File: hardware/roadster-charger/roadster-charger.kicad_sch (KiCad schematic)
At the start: 63 parts, among them J1 USB4505-03-0-A, J2 USB4505-03-0-A, J3 54-00166, Q1 CSD19532Q5B, U1 MPM3606AGQV-P, U2 ESP32-C3-MINI-1, U3 INA168, U4 OPA340NA, U5 FUSB307BMPX, U6 LM75B, U7 LM5050-1, U8 INA168, U9 OPA340NA

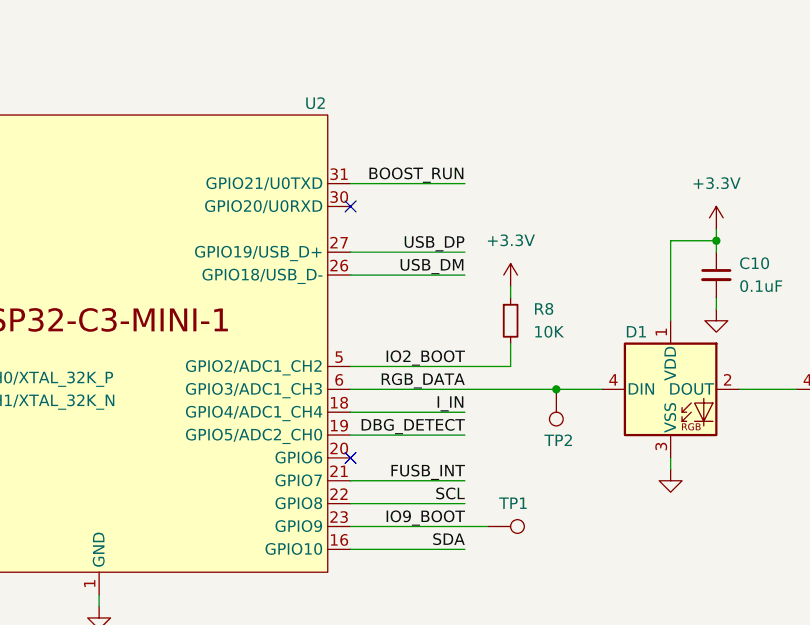
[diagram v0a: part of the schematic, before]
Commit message: Rough rev 2 layout
Move boost run pin to GPIO6 to avoid hard coded UART output
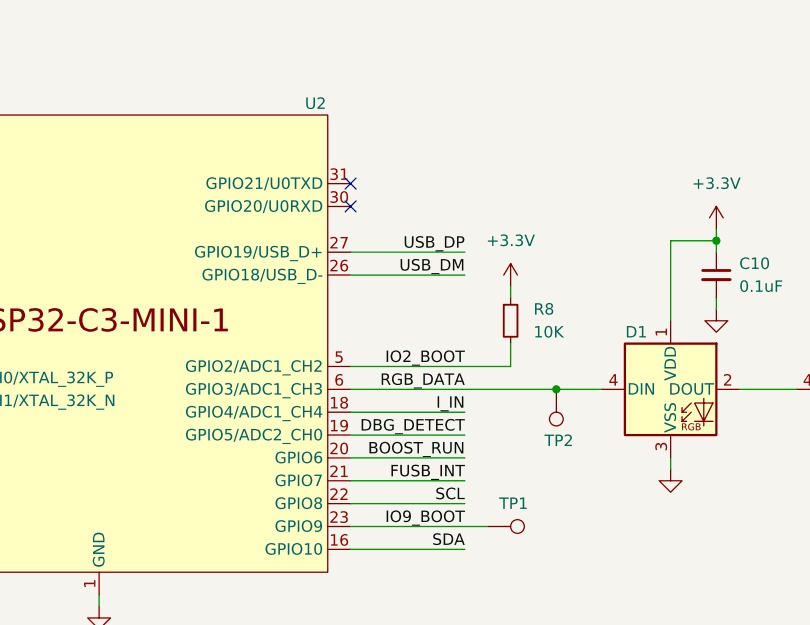
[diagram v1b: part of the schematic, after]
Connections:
- net BOOST_RUN: now also U2.20 (GPIO6); no longer U2.31 (GPIO21/U0TXD)
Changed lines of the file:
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@@
 	)
 	(no_connect
-		(at 96.52 227.33)
+		(at 96.52 196.85)
 	)
 	(no_connect
@@
 	(wire
 		(pts
-			(xy 96.52 196.85) (xy 109.22 196.85)
-		)
-		(stroke
-			(width 0)
-			(type default)
-		)
-	)
-	(wire
-		(pts
 			(xy 387.35 140.97) (xy 387.35 143.51)
 		)
@@
 	(wire
 		(pts
+			(xy 96.52 227.33) (xy 109.22 227.33)
+		)
+		(stroke
+			(width 0)
+			(type default)
+		)
+	)
+	(wire
+		(pts
 			(xy 36.83 241.3) (xy 36.83 238.76)
 		)
@@
 	)
 	(label "BOOST_RUN"
-		(at 109.22 196.85 180)
+		(at 109.22 227.33 180)
 		(fields_autoplaced yes)
 		(effects
@@
 			)
 		)
-		(property "Description" "\nConnector, dc jack 5.5x2.1 mm, PCB mount, 90 degrees, nickel plated, PBT, thru hole\n"
+		(property "Description" "Connector, dc jack 5.5x2.1 mm, PCB mount, 90 degrees, nickel plated, PBT, thru hole"
 			(at 393.7 140.97 0)
 			(effects

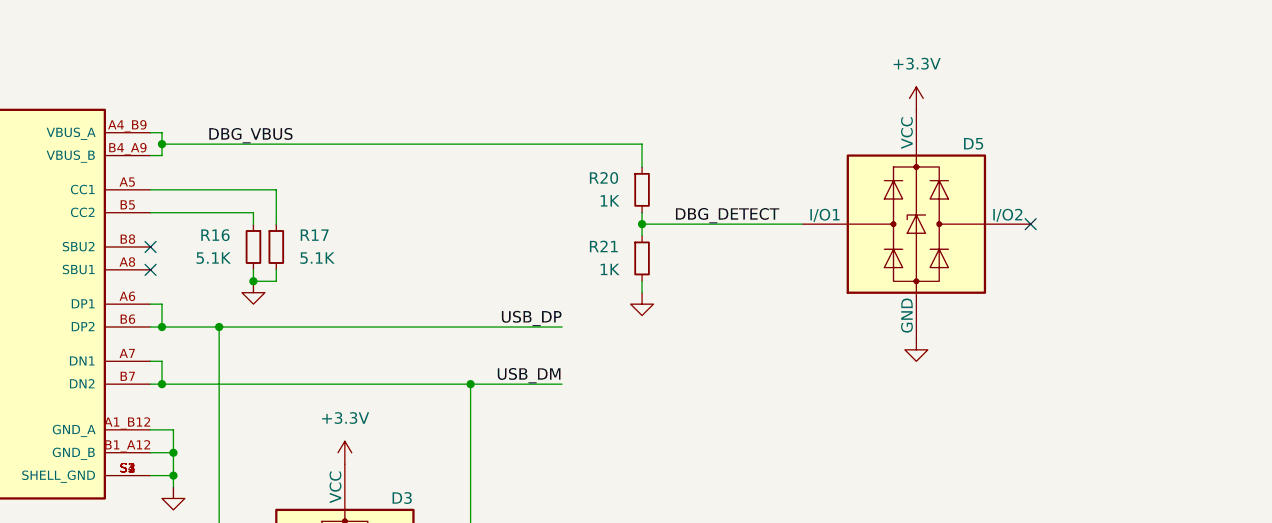
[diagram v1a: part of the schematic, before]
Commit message: add debug connected LED
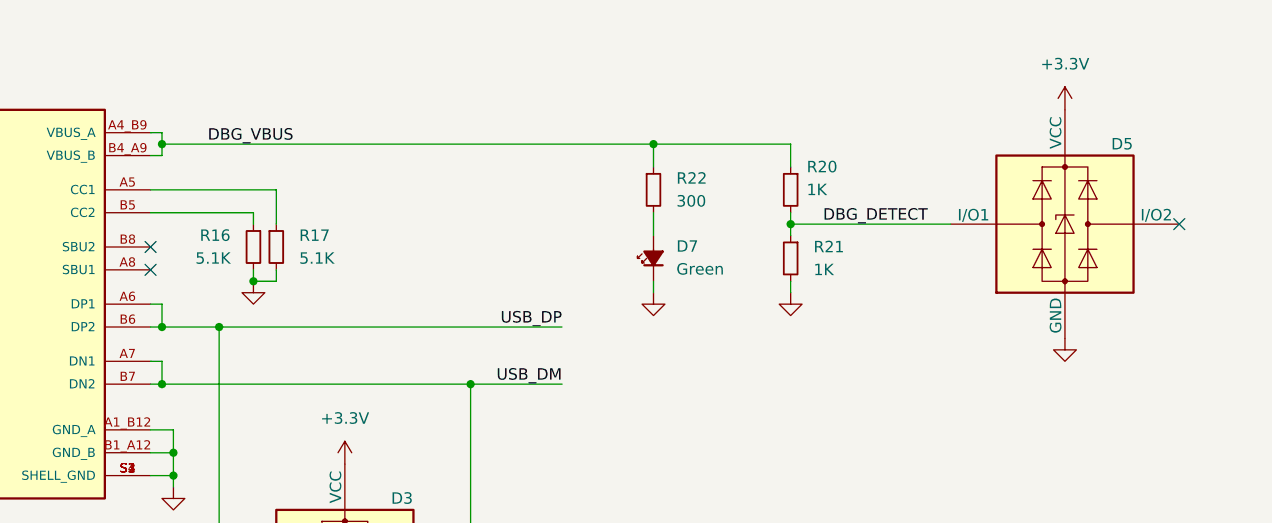
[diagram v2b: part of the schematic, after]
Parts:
- added D7: Green, LED_SMD:LED_0805_2012Metric, symbol Device:LED_Small_Filled
- added R22: 300, Resistor_SMD:R_0603_1608Metric, symbol Device:R_Small
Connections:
- net DBG_VBUS: now also R22.1
- net GND: now also D7.1 (K)
- new net: D7.2 (A), R22.2
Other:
- moved on the sheet: D5, R20, R21

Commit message: change all 1K Rs to 0.1%, invert DAC jumpers
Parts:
- R19, R20, R21: MPN RC0603FR-071KL -> RT0603BRD071KL
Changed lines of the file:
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@@
 			)
 		)
-		(property "MPN" "RC0603FR-071KL"
+		(property "MPN" "RT0603BRD071KL"
 			(at 360.68 36.83 0)
 			(effects
@@
 			)
 		)
-		(property "MPN" "RC0603FR-071KL"
+		(property "MPN" "RT0603BRD071KL"
 			(at 340.36 168.91 0)
 			(effects
@@
 			)
 		)
-		(property "MPN" "RC0603FR-071KL"
+		(property "MPN" "RT0603BRD071KL"
 			(at 360.68 44.45 0)
 			(effects

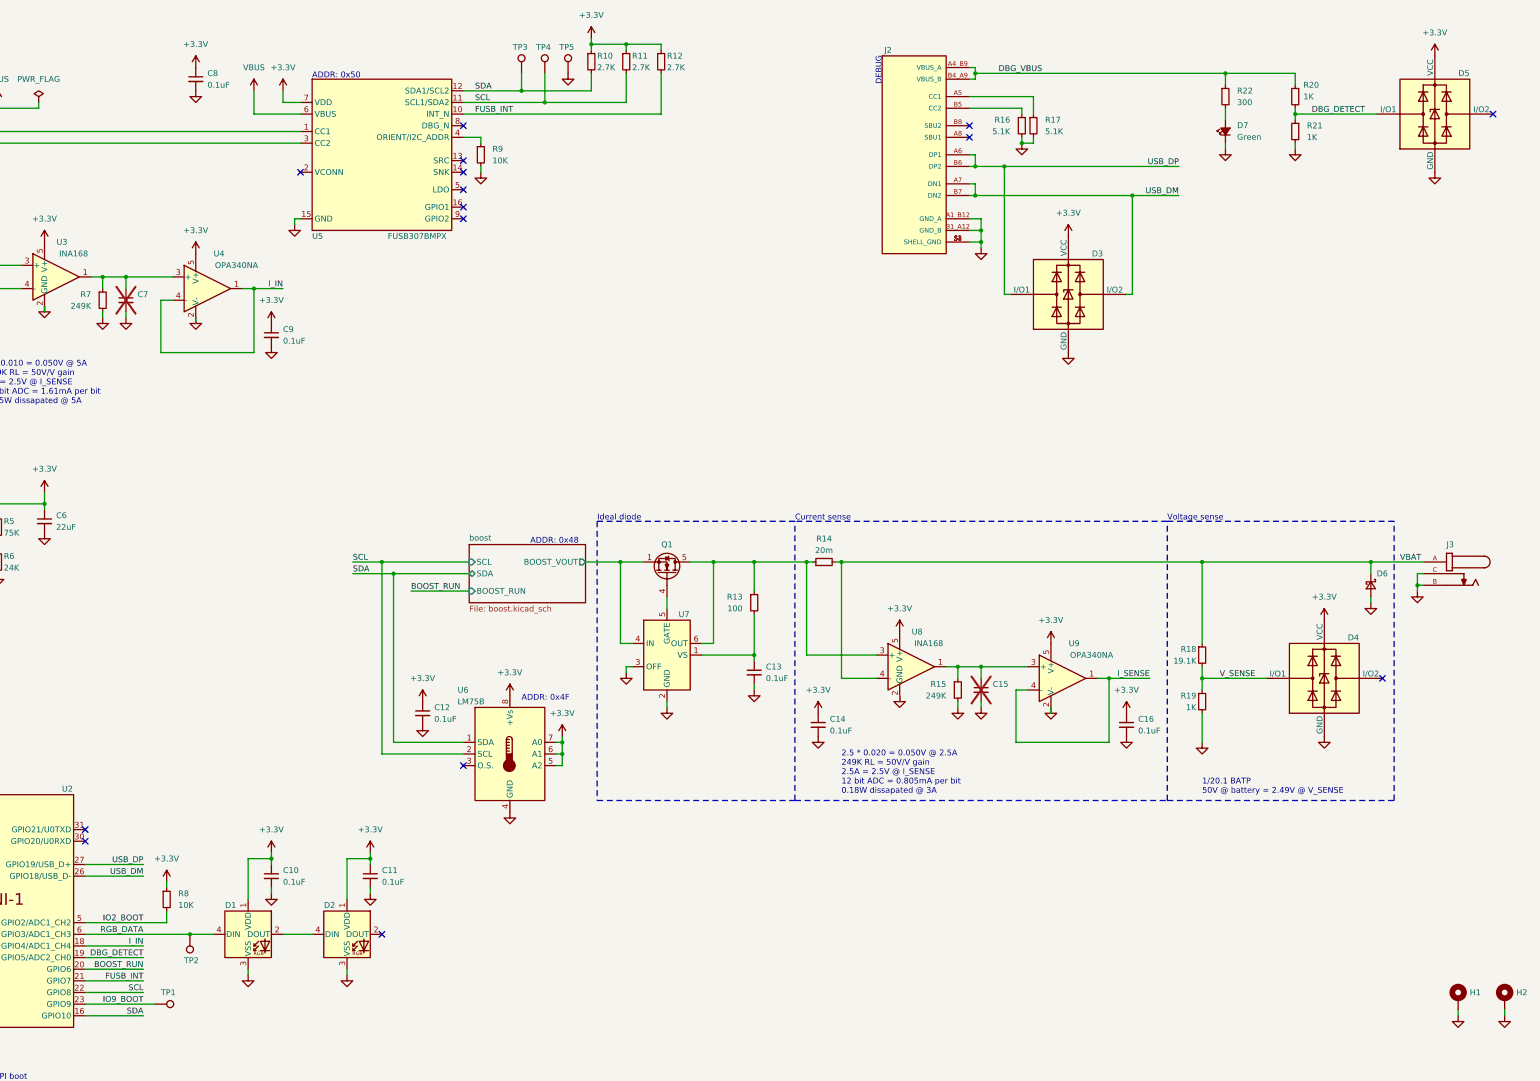
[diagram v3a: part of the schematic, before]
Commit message: reannotate, add uart test points
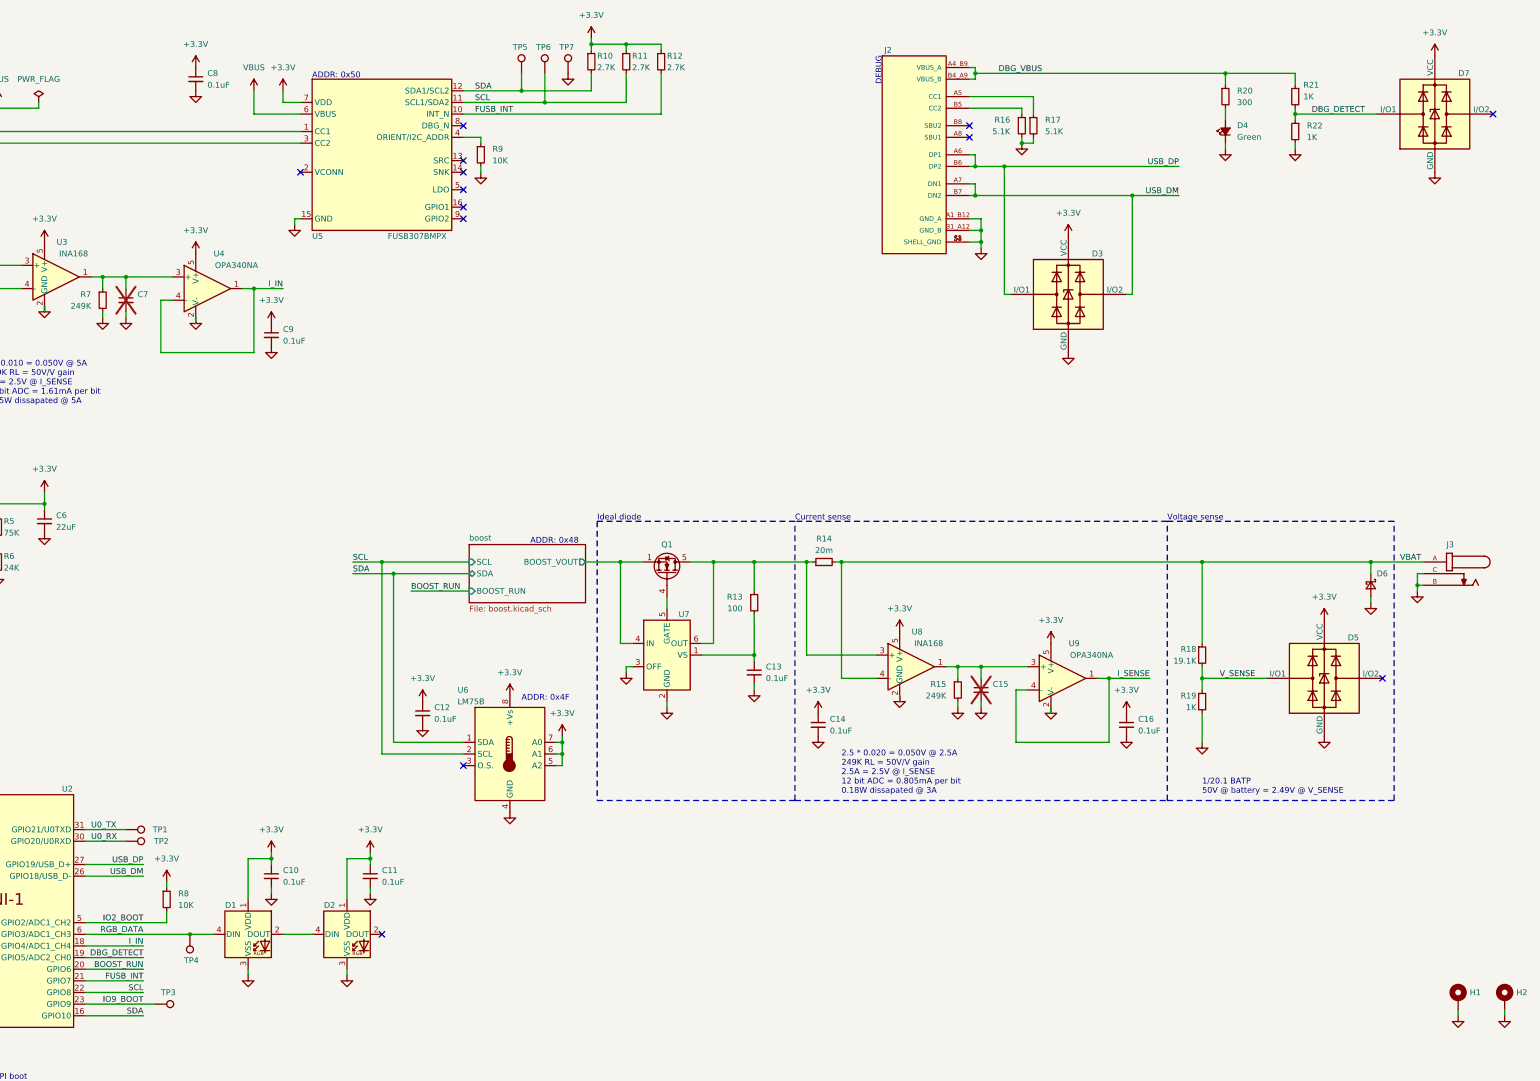
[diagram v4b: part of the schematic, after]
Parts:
- added TP1, TP2: RCU-0C, RCU-0C:TP+195X110, symbol Connector:TestPoint
- renumbered D7 to D4, D4 to D5, D5 to D7, R22 to R20, R20 to R21, R21 to R22, TP1 to TP3, TP2 to TP4, TP3 to TP5, TP4 to TP6, TP5 to TP7
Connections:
- net U0_RX: now reaches U2.30 (GPIO20/U0RXD)
- net U0_RX: now also TP2.1
- net U0_TX: now reaches U2.31 (GPIO21/U0TXD)
- net U0_TX: now also TP1.1
- no-connect marks 23 -> 21

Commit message: use track cleanup tool
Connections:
- net GND: no longer J1.S1 (SHELL_GND), J1.S2 (SHELL_GND), J1.S3 (SHELL_GND), J1.S4 (SHELL_GND), J2.S1 (SHELL_GND), J2.S2 (SHELL_GND), J2.S3 (SHELL_GND), J2.S4 (SHELL_GND)
- new net: J2.S1 (SHELL_GND), J2.S2 (SHELL_GND), J2.S3 (SHELL_GND), J2.S4 (SHELL_GND)
- new net: J1.S1 (SHELL_GND), J1.S2 (SHELL_GND), J1.S3 (SHELL_GND), J1.S4 (SHELL_GND)
- no-connect marks 21 -> 23
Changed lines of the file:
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@@
-	)
-	(junction
-		(at 292.1 68.58)
-		(diameter 0)
-		(color 0 0 0 0)
 	)
 	(junction
@@
 	(junction
 		(at 345.44 31.75)
-		(diameter 0)
-		(color 0 0 0 0)
-	)
-	(junction
-		(at 60.96 76.2)
 		(diameter 0)
 		(color 0 0 0 0)
@@
 	)
 	(no_connect
+		(at 58.42 76.2)
+	)
+	(no_connect
 		(at 179.07 60.96)
+	)
+	(no_connect
+		(at 289.56 68.58)
 	)
 	(no_connect
@@
 	(wire
 		(pts
-			(xy 60.96 76.2) (xy 60.96 77.47)
+			(xy 60.96 73.66) (xy 60.96 77.47)
 		)
 		(stroke
@@
 	(wire
 		(pts
-			(xy 292.1 66.04) (xy 292.1 68.58)
+			(xy 292.1 66.04) (xy 292.1 69.85)
 		)
 		(stroke
@@
 	(wire
 		(pts
-			(xy 289.56 68.58) (xy 292.1 68.58)
-		)
-		(stroke
-			(width 0)
-			(type default)
-		)
-	)
-	(wire
-		(pts
 			(xy 137.16 203.2) (xy 137.16 204.47)
 		)
@@
 		)
 		(stroke
-			(width 0)
-			(type default)
-		)
-	)
-	(wire
-		(pts
-			(xy 58.42 76.2) (xy 60.96 76.2)
-		)
-		(stroke
-			(width 0)
-			(type default)
-		)
-	)
-	(wire
-		(pts
-			(xy 292.1 68.58) (xy 292.1 69.85)
-		)
-		(stroke
-			(width 0)
-			(type default)
-		)
-	)
-	(wire
-		(pts
-			(xy 60.96 73.66) (xy 60.96 76.2)
-		)
-		(stroke

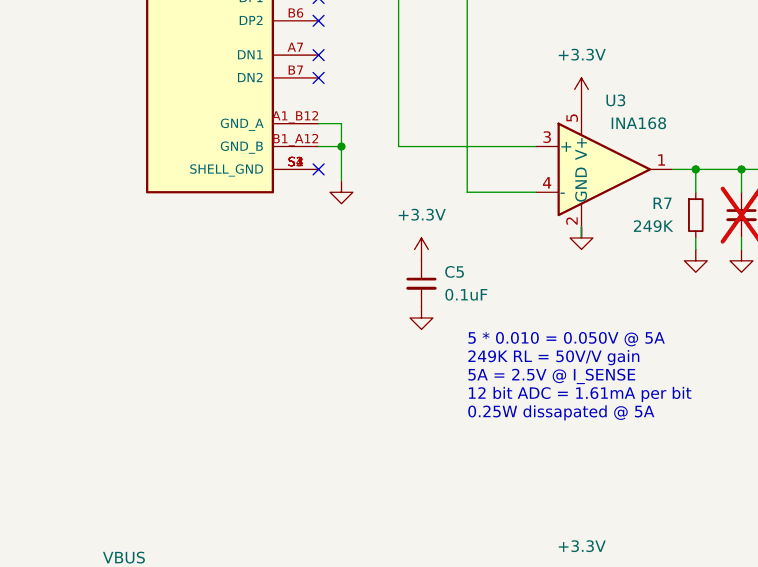
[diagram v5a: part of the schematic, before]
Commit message: ERC / DRC cleanup
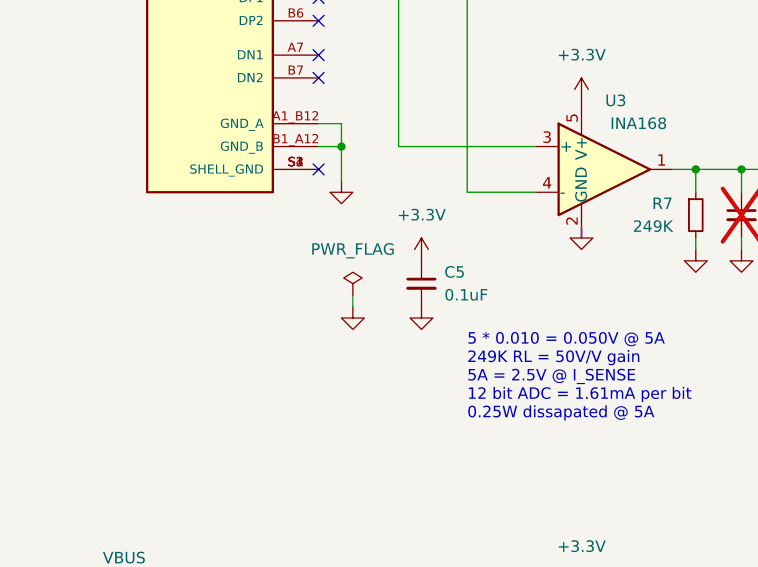
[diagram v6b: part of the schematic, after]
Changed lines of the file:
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@@
 		)
 	)
+	(wire
+		(pts
+			(xy 62.23 90.17) (xy 62.23 91.44)
+		)
+		(stroke
+			(width 0)
+			(type default)
+		)
+	)
 	(polyline
 		(pts
@@
 	)
 	(symbol
+		(lib_id "power:GND")
+		(at 62.23 91.44 0)
+		(unit 1)
+		(exclude_from_sim no)
+		(in_bom yes)
+		(on_board yes)
+		(dnp no)
+		(property "Reference" "#PWR089"
+			(at 62.23 97.79 0)
+			(effects
+				(font
+					(size 1.27 1.27)
+				)
+				(hide yes)
+			)
+		)
+		(property "Value" "GND"
+			(at 62.23 96.52 0)
+			(effects
+				(font
+					(size 1.27 1.27)
+				)
+				(hide yes)
+			)
+		)
+		(property "Footprint" ""
+			(at 62.23 91.44 0)
+			(effects
+				(font
+					(size 1.27 1.27)
+				)
+				(hide yes)
+			)
+		)
+		(property "Datasheet" ""
+			(at 62.23 91.44 0)
+			(effects
+				(font
+					(size 1.27 1.27)
+				)
+				(hide yes)
+			)
+		)
+		(property "Description" ""
+			(at 62.23 91.44 0)
+			(effects
+				(font
+					(size 1.27 1.27)
+				)
+				(hide yes)
+			)
+		)
+		(pin "1"
+		)
+		(instances
+			(project "roadster-charger"
+				(path "/57ecac41-cd8a-4182-a81e-fed3e381aedd"
+					(reference "#PWR089")
+					(unit 1)
+				)
+			)
+		)
+	)
+	(symbol
 		(lib_id "power:+3.3V")
 		(at 114.3 208.28 0)
@@
 	(symbol
 		(lib_id "power:PWR_FLAG")
+		(at 62.23 90.17 0)
+		(unit 1)
+		(exclude_from_sim no)
+		(in_bom yes)
+		(on_board yes)
+		(dnp no)
+		(fields_autoplaced yes)
+		(property "Reference" "#FLG02"
+			(at 62.23 88.265 0)
+			(effects
+				(font
+					(size 1.27 1.27)
+				)
+				(hide yes)
+			)
+		)
+		(property "Value" "PWR_FLAG"
+			(at 62.23 85.09 0)
+			(effects
+				(font
+					(size 1.27 1.27)
+				)
+			)
+		)
+		(property "Footprint" ""
+			(at 62.23 90.17 0)
+			(effects
+				(font
+					(size 1.27 1.27)
+				)
+				(hide yes)
+			)
+		)
+		(property "Datasheet" "~"
+			(at 62.23 90.17 0)
+			(effects
+				(font
+					(size 1.27 1.27)
+				)
+				(hide yes)
+			)
+		)
+		(property "Description" ""
+			(at 62.23 90.17 0)
+			(effects
+				(font
+					(size 1.27 1.27)
+				)
+				(hide yes)
+			)
+		)
+		(pin "1"
+		)
+		(instances
+			(project "roadster-charger"
+				(path "/57ecac41-cd8a-4182-a81e-fed3e381aedd"
+					(reference "#FLG02")
+					(unit 1)
+				)
+			)
+		)
+	)
+	(symbol
+		(lib_id "power:PWR_FLAG")
 		(at 86.36 38.1 0)
 		(unit 1)
@@
 	)
 	(symbol
+		(lib_name "WS2812B_1")
 		(lib_id "LED:WS2812B")
 		(at 132.08 219.71 0)

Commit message: Fix res PN, remove TPs from BOM, add DNPs to BOM
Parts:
- C15, C7: now in the parts list
- H1, H2: MPN (none) -> DNP
- R20: MPN (none) -> RC0603JR-07330RL; MPN  RC0603JR-07330RL -> (none)
- TP1, TP2, TP3, TP4, TP5, TP6, TP7: now left out of the parts list
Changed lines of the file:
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@@
 		(unit 1)
 		(exclude_from_sim no)
-		(in_bom yes)
+		(in_bom no)
 		(on_board yes)
 		(dnp no)
@@
 		(unit 1)
 		(exclude_from_sim no)
-		(in_bom yes)
+		(in_bom no)
 		(on_board yes)
 		(dnp no)
@@
 			)
 		)
-		(property "MPN " "RC0603JR-07330RL"
+		(property "MPN" "RC0603JR-07330RL"
 			(at 345.44 36.83 0)
 			(effects
@@
 			)
 		)
+		(property "MPN" "DNP"
+			(at 406.4 233.68 0)
+			(effects
+				(font
+					(size 1.27 1.27)
+				)
+				(hide yes)
+			)
+		)
 		(pin "1"
 		)
@@
 		(unit 1)
 		(exclude_from_sim no)
-		(in_bom no)
+		(in_bom yes)
 		(on_board yes)
 		(dnp yes)
@@
 		(unit 1)
 		(exclude_from_sim no)
-		(in_bom yes)
+		(in_bom no)
 		(on_board yes)
 		(dnp no)
@@
 		(unit 1)
 		(exclude_from_sim no)
-		(in_bom yes)
+		(in_bom no)
 		(on_board yes)
 		(dnp no)
@@
 		(unit 1)
 		(exclude_from_sim no)
-		(in_bom no)
+		(in_bom yes)
 		(on_board yes)
 		(dnp yes)
@@
 		(unit 1)
 		(exclude_from_sim no)
-		(in_bom yes)
+		(in_bom no)
 		(on_board yes)
 		(dnp no)
@@
 		(unit 1)
 		(exclude_from_sim no)
-		(in_bom yes)
+		(in_bom no)
 		(on_board yes)
 		(dnp no)
@@
 		(unit 1)
 		(exclude_from_sim no)
-		(in_bom yes)
+		(in_bom no)
 		(on_board yes)
 		(dnp no)
@@
 			(at 396.24 233.68 0)
 			(effects
+				(font
+					(size 1.27 1.27)
+				)
+				(hide yes)
+			)
+		)
+		(property "MPN" "DNP"
+			(at 396.24 233.68 0)
+			(effects

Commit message: Change bom output to CSV
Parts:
- H1, H2: now left out of the parts list
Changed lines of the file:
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@@
 		(unit 1)
 		(exclude_from_sim no)
-		(in_bom yes)
+		(in_bom no)
 		(on_board yes)
 		(dnp no)
@@
 		(unit 1)
 		(exclude_from_sim no)
-		(in_bom yes)
+		(in_bom no)
 		(on_board yes)
 		(dnp no)
